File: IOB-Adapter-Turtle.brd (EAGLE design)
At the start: 17.8 x 38.1 mm, 5 parts

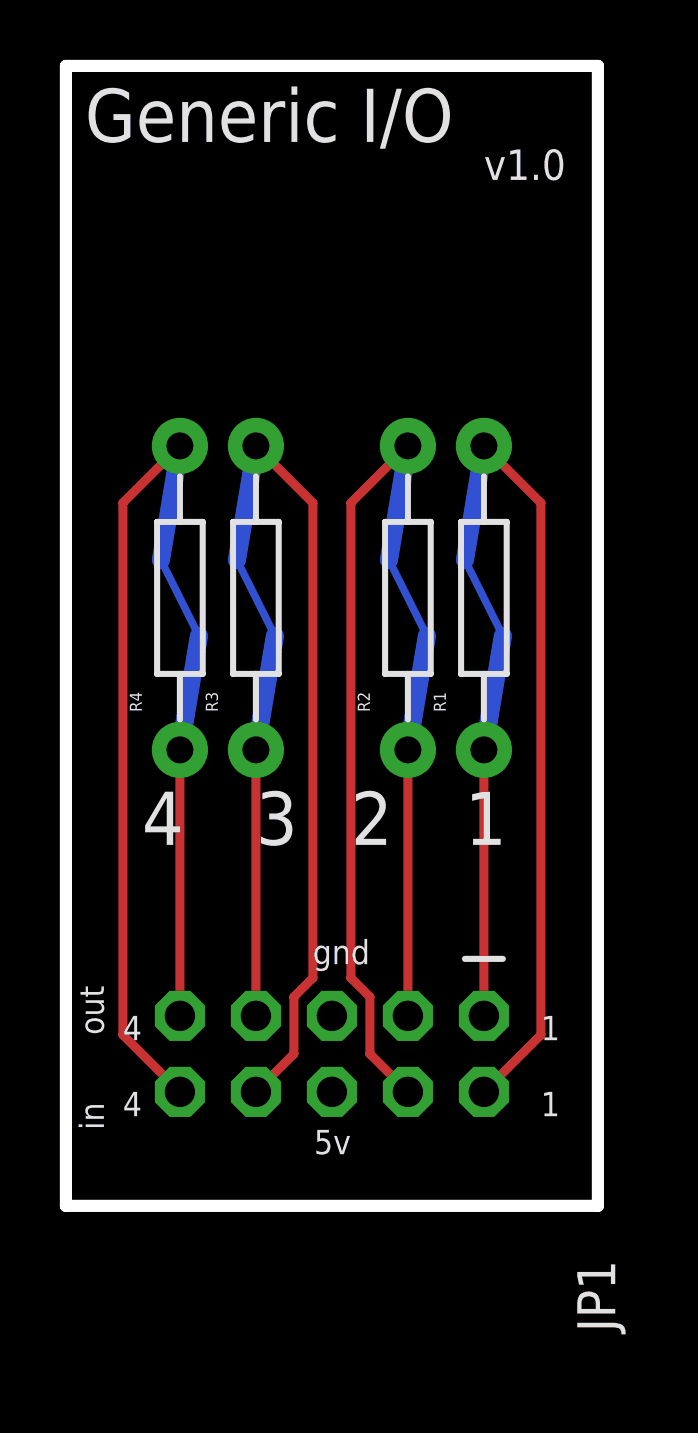
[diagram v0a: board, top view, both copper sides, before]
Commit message: silkscreen tweeks
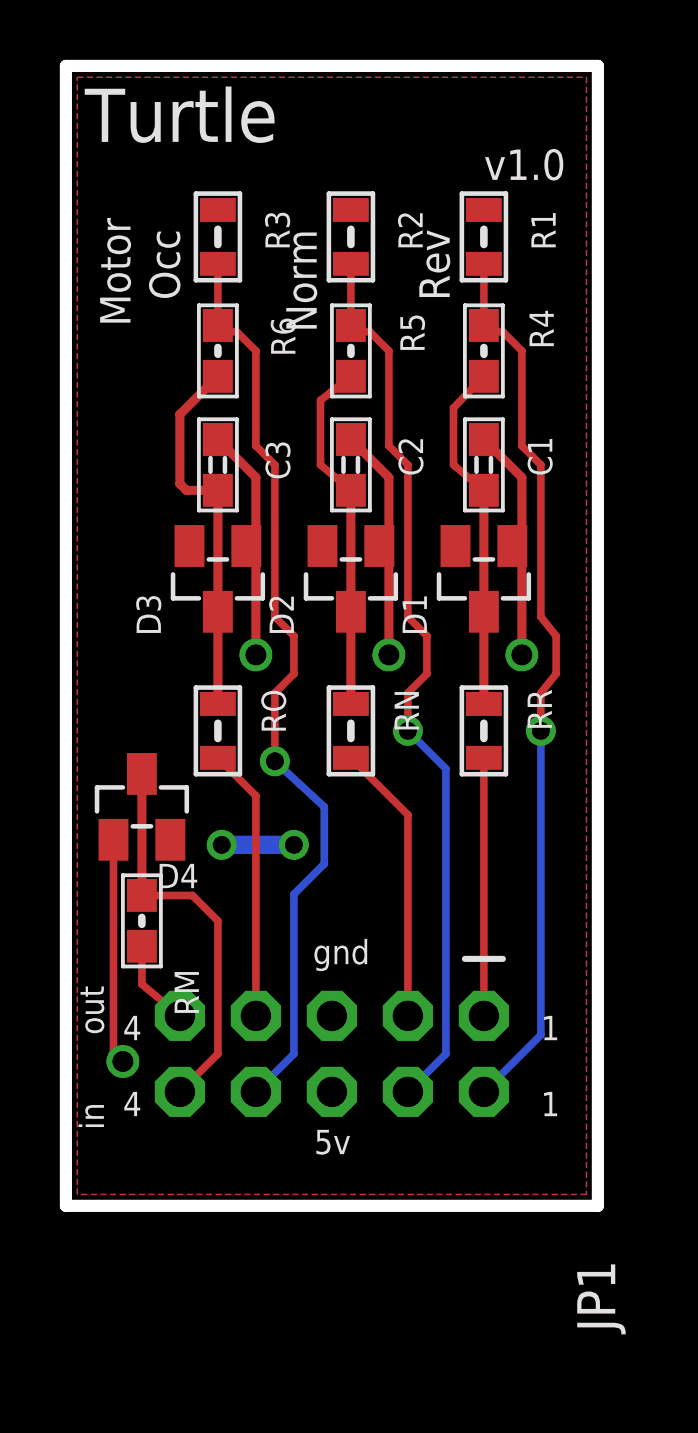
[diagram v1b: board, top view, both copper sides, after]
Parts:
- added C1, C2, C3: 0.01uF, SPCoast:0603-CAP
- added D1, D2, D3: BAT54S, SPCoast:SOT23
- added D4: 4.7v, SPCoast:SOT23
- added R5, R6, RM: 1K0, SPCoast:0603-RES
- added RN, RO, RR: 82R, SPCoast:0805-RES
- R1, R2, R3: value NOSTUFF -> 10k; device SPCoast:CUT-R -> SPCoast:0805-RES
- R4: value NOSTUFF -> 1K0; device SPCoast:CUT-R -> SPCoast:0603-RES
- moved R4 13.1 mm to (14.0, 28.6), turned to 270 degrees
- moved R2 12.2 mm to (9.53, 32.4), turned to 270 degrees
- moved R3 12.1 mm to (5.08, 32.4), turned to 270 degrees
- moved R1 12.1 mm to (14.0, 32.4), turned to 270 degrees
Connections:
- removed net N$1: JP1.1, R1.P2
- removed net N$4: JP1.9, R4.P2
- new net IO1: JP1.1, RR.2
- new net IO2: JP1.3, RN.2
- new net IO3: JP1.7, RO.2
- new net IO4: JP1.9, RM.1
- new net N$14: C3.1, D3.3, R6.2, RO.1
- net GND: now also C1.2, C2.2, C3.2, D1.1, D2.1, D3.1, D4.1
- net N$2: now also C2.1, D2.3, R5.2, RN.1; no longer JP1.3, R2.P2
- net N$3: now also C1.1, D1.3, R4.2, RR.1; no longer JP1.7, R3.P2
- net P1: now also R1.2, R4.1; no longer R1.P1
- net P2: now also R2.2, R5.1; no longer R2.P1
- net P3: now also R3.2, R6.1; no longer R3.P1
- net P4: now also D4.3, RM.2; no longer R4.P1
- net VCC: now also D1.2, D2.2, D3.2, R1.1, R2.1, R3.1
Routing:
- net GND: track 0.00 -> 32.5 mm, vias 0 -> 4
- net N$14: track 0.00 -> 12.6 mm
- net P4: track 23.2 -> 13.2 mm
- net IO2: track 0.00 -> 9.41 mm
- net IO3: track 0.00 -> 9.15 mm
- net N$4: track 8.89 -> 0.00 mm
- net N$1: track 8.89 -> 0.00 mm
- net IO1: track 0.00 -> 8.62 mm
- net P3: track 23.2 -> 30.9 mm, vias 0 -> 1
- net P2: track 23.2 -> 30.3 mm, vias 0 -> 1
- net P1: track 23.2 -> 29.9 mm, vias 0 -> 1
- net N$2: track 8.89 -> 11.9 mm
- net N$3: track 8.89 -> 11.8 mm
- net IO4: track 0.00 -> 2.92 mm
- net VCC: track 0.00 -> 2.41 mm, vias 0 -> 2
- added copper zone on layer 16, net GND
- added copper zone on layer 1, net VCC
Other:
- board text added: "C1"
- board text added: "C2"
- board text added: "C3"
- board text added: "D1"
- board text added: "D2"
- board text added: "D3"
- board text added: "D4"
- board text added: "Green"
- board text added: "Motor"
- board text added: "Norm"
- board text added: "Occ"
- board text added: "R5"
- board text added: "R6"
- board text added: "RM"
- board text added: "RN"
- board text added: "RO"
- board text added: "RR"
- board text added: "Rev"
- board text added: "Turtle"
- board text removed: "1"
- board text removed: "2"
- board text removed: "3"
- board text removed: "4"
- board text removed: "Cut traces if using resistors"
- board text removed: "GENERIC I/O"
- board text removed: "Generic I/O"
- board text removed: "Yellow"
